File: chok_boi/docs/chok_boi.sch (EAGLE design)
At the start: 13 parts

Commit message: Add gyro and update MOSFETS
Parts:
- removed C_3.3V_IN, C_3.3V_NR, C_BAT: 0.1uF, SparkFun:CAP0603-CAP
- removed C_3.3V_OUT: 10uF, SparkFun:CAP0603-CAP
- removed C_5V: 100uF, SparkFun:CAP0603-CAP
- added B0, B1: (no value), SparkFun-Retired:TAC_SWITCHSMD
- added C_3.3V1: 10uF, SparkFun:CAP0603-CAP
- added C_3.3V2, C_5V1, C_5V11, C_5V4, C_5V5, C_5V6, C_5V7, C_5V8, C_5V9, C_NR, C_NRST, C_VDD1, C_VDD3, C_VDDA1: 0.1uF, SparkFun:CAP0603-CAP
- added C_5V10: 0.01uF, SparkFun:CAP0603-CAP
- added C_5V12: 2.2nF, SparkFun:CAP0603-CAP
- added C_5V2, C_BAT2: 100uF, SparkFun-Passives:CAP1206
- added C_BAT1, C_ELF2, C_ERF2, C_ERF3, C_S2, C_VDD0, C_VDD2: 0.1uF, SparkFun-Capacitors:CAP0603-CAP
- added C_ELF1, C_ERF1, C_ERF4, C_S1: 4.7uF, SparkFun-Capacitors:CAP0603-CAP
- added C_VCAP1, C_VCAP2: 2.2uF, SparkFun:CAP0603-CAP
- added C_VDDA2: 1uF, SparkFun:CAP0603-CAP
- added C_VSS1: 4.7uF, SparkFun:CAP0603-CAP
- added IC1: L293DD, st-microelectronics:L293DD
- added LED1, LED2, LED3: (no value), SparkFun:LED0603
- added LED_PWR: green, SparkFun:LED1206
- added R_B0, R_BOOT1, R_ELF_PD, R_ERF_PD, R_ERF_PD1, R_ES_PD: 47k, SparkFun-Passives:RESISTOR0603-RES
- added R_ELF, R_ERF: 10, SparkFun-Passives:RESISTOR0603-RES
- added R_ES1, R_ES2, R_ES3, R_ES4: 5.6, SparkFun-Passives:RESISTOR0603-RES
- added R_LED1, R_LED2, R_LED3, R_PWR: 1k, SparkFun-Passives:RESISTOR0603-RES
- added R_RLF, R_RLS, R_RRF, R_RRF1, R_RRF2, R_RRS: 1.8k, SparkFun-Passives:RESISTOR0603-RES
- added R_VM1: 20k, SparkFun-Passives:RESISTOR0603-RES
- added R_VM2: 10k, SparkFun-Passives:RESISTOR0603-RES
- added SERIAL1, SERIAL2: (no value), pinhead:PINHD-1X4
- added T1, T2, T3, T4: (no value), zetex:NPNSOT323
- added U$10, U$11, U$13, U$17, U$18, U$19: EMITTER, sfh4550 _ teft4300:EMITTER
- added U$12: FUTURA_V1.0_MOTOR_MOUNT, Futura 1.0 motor mount template:FUTURA_V1.0_MOTOR_MOUNT
- added U$15, U$16: SPLITTER, splitter:SPLITTER
- added U$20, U$21, U$7, U$8, U$9: RECEIVER, sfh4550 _ teft4300:RECEIVER
- added U1: MPU-6000, SparkFun-Sensors:MPU-6000
- L1: device SparkFun:INDUCTOR1007 -> SparkFun-Passives:INDUCTOR1007
- S1: device SparkFun-Switches:SWITCH-SPDT-PTH-11.6X4.0MM -> SparkFun:SWITCH-SPSTPTH
- U$1: value TPS76850(SOIC-8) -> JST_CONNECTOR_FEMALE; device TPS76850(SOIC-8):TPS76850(SOIC-8) -> JST_CONNECTOR_FEMALE. through hole:JST_CONNECTOR_FEMALE
- U$2: value TPS73633(SOT-23) -> JST_CONNECTOR_FEMALE; device TPS73633(SOT-23):TPS73633(SOT-23) -> JST_CONNECTOR_FEMALE. through hole:JST_CONNECTOR_FEMALE
- U$3: value JST_CONNECTOR_FEMALE -> TPS73633(SOT-23); device JST_CONNECTOR_FEMALE. through hole:JST_CONNECTOR_FEMALE -> TPS73633(SOT-23):TPS73633(SOT-23)
- U$4: value JST_CONNECTOR_FEMALE -> TPS76850(SOIC-8); device JST_CONNECTOR_FEMALE. through hole:JST_CONNECTOR_FEMALE -> TPS76850(SOIC-8):TPS76850(SOIC-8)
- U$5: value SPLITTER -> STM32F405/415_LQFP64; device splitter:SPLITTER -> STM32F10x F4xx:STM32F405/415_LQFP64
- U$6: value SPLITTER -> RECEIVER; device splitter:SPLITTER -> sfh4550 _ teft4300:RECEIVER
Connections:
- removed net BAT: C_BAT.1, S1.S, U$1.IN1, U$1.IN2
- new net BATTERY: C_BAT1.1, C_BAT2.1, IC1.VS, R_VM1.2, S1.P, U$4.IN1, U$4.IN2
- new net BOOT0: B0.4, R_B0.1, U$5.BOOT0, U$5.PB5
- new net EM_D: R_ES_PD.2, T2.B, U$5.PA5
- new net EM_LF: R_ELF_PD.2, T1.B, U$5.PC6
- new net EM_RF: R_ERF_PD.2, T3.B, U$5.PA2
- new net EM_S: R_ERF_PD1.2, T4.B
- new net ENC_LA: U$12.L_CHA, U$5.PA15
- new net ENC_LB: U$12.L_CHB, U$5.PB3
- new net ENC_RA: U$12.R_CHA, U$5.PA0_AKUP
- new net ENC_RB: U$12.R_CHB, U$5.PA1
- new net INT: U1.INT
- new net LED1: LED1.A, U$5.PA11
- new net LED2: LED2.A, U$5.PC10
- new net LED3: LED3.A, U$5.PC0
- new net MISO: U1.AD0/SDO
- new net MLB: IC1.OUT1, U$12.L_MOTOR_B
- new net MLF: IC1.OUT2, U$12.L_MOTOR_A
- new net MOSI: U1.SDA/SDI
- new net MRB: IC1.OUT3, U$12.R_MOTOR_B
- new net MRF: IC1.OUT4, U$12.R_MOTOR_A
- new net N$10: R_BOOT1.1, U$5.PB2
- new net N$12: LED1.C, R_LED1.2
- new net N$14: U$18.-, U$19.+
- new net N$15: R_ES3.2, R_ES4.2, U$19.-
- new net N$16: LED2.C, R_LED2.2
- new net N$17: R_ES1.2, R_ES2.2, U$17.-
- new net N$18: R_ES1.1, R_ES2.1, T2.C
- new net N$19: R_ES3.1, R_ES4.1, T4.C
- new net N$20: C_5V11.1, U1.REGOUT
- new net N$21: LED3.C, R_LED3.2
- new net N$22: C_5V12.1, U1.CPOUT
- new net N$23: R_ERF.1, T3.C
- new net N$27: R_ERF.2, U$13.-
- new net N$4: C_VCAP1.2, U$5.VCAP_1
- new net N$5: R_ELF.2, U$10.-
- new net N$6: C_VCAP2.2, U$5.VCAP_2
- new net N$7: R_ELF.1, T1.C
- new net N$8: LED_PWR.A, R_PWR.1
- new net N$9: U$11.-, U$17.+
- new net OUTZ: U$5.PA7
- new net PWMLB: IC1.IN1, U$5.PB7
- new net PWMLF: IC1.IN2, U$5.PB6
- new net PWMRB: IC1.IN3, U$5.PB8
- new net PWMRF: IC1.IN4, U$5.PB9
- new net REC_LD: R_RLS.2, U$5.PC4, U$7.E
- new net REC_LF: R_RLF.2, U$5.PC5, U$6.E
- new net REC_LH: R_RRF2.2, U$21.E
- new net REC_RD: R_RRS.2, U$5.PA6, U$8.E
- new net REC_RF: R_RRF.2, U$5.PA4, U$9.E
- new net REC_RH: R_RRF1.2, U$20.E
- new net RESET: B1.3, C_NRST.1, SERIAL2.4, U$5.NRST
- new net RX: SERIAL1.2, U$5.PA10
- new net SCK: U1.SCL/SCLK
- new net SS1: U1.CS
- new net SWCLK: SERIAL2.1, U$5.PA14
- new net SWDIO: SERIAL2.3, U$5.PA13
- new net TX: SERIAL1.1, U$5.PA9
- new net VOLTMETER: R_VM1.1, R_VM2.2, U$5.PA3
- net 3.3V: now also B0.1, C_3.3V1.1, C_3.3V2.1, C_VDD0.2, C_VDD1.2, C_VDD2.1, C_VDD3.1, C_VSS1.1, L1.1, SERIAL1.4, U$3.OUT, U$5.VBAT, U$5.VDD_0, U$5.VDD_1, U$5.VDD_2, U$5.VDD_3; no longer C_3.3V_OUT.1, L1.2, U$2.OUT
- net 5V: now also C_5V1.1, C_5V2.1, C_ELF1.1, C_ELF2.1, C_ERF1.1, C_ERF2.1, C_ERF3.1, C_ERF4.1, C_S1.1, C_S2.1, IC1.EN1, IC1.EN2, IC1.VSS, R_PWR.2, U$10.+, U$11.+, U$12.L_VCC, U$12.R_VCC, U$13.+, U$18.+, U$3.EN, U$3.IN, U$4.OUT1, U$4.OUT2; no longer C_3.3V_IN.1, C_5V.1, U$1.OUT1, U$1.OUT2, U$2.EN, U$2.IN
- net A3.3V: now also C_5V10.1, C_5V4.1, C_5V5.1, C_5V6.1, C_5V7.1, C_5V8.1, C_5V9.1, C_VDDA1.1, C_VDDA2.1, L1.2, U$20.C, U$21.C, U$5.VDDA, U$6.C, U$7.C, U$8.C, U$9.C, U1.VDD; no longer L1.1
- net AGND: now also C_5V10.2, C_5V11.2, C_5V12.2, C_5V4.2, C_5V5.2, C_5V6.2, C_5V7.2, C_5V8.2, C_5V9.2, C_VDDA1.2, C_VDDA2.2, R_RLF.1, R_RLS.1, R_RRF.1, R_RRF1.1, R_RRF2.1, R_RRS.1, U$15.2, U$5.VSSA, U1.GND; no longer U$6.2
- net GND: now also B1.2, C_3.3V1.2, C_3.3V2.2, C_5V1.2, C_5V2.2, C_BAT1.2, C_BAT2.2, C_ELF1.2, C_ELF2.2, C_ERF1.2, C_ERF2.2, C_ERF3.2, C_ERF4.2, C_NR.2, C_NRST.2, C_S1.2, C_S2.2, C_VCAP1.1, C_VCAP2.1, C_VDD0.1, C_VDD1.1, C_VDD2.2, C_VDD3.2, C_VSS1.2, LED_PWR.C, R_B0.2, R_BOOT1.2, R_ELF_PD.1, R_ERF_PD.1, R_ERF_PD1.1, R_ES_PD.1, R_LED1.1, R_LED2.1, R_LED3.1, R_VM2.1, SERIAL1.3, SERIAL2.2, T1.E, T2.E, T3.E, T4.E, U$1.-, U$12.L_GND, U$12.R_GND, U$15.1, U$16.2, U$3.GND, U$4.EN(BAR), U$4.GND, U$5.VSS_0, U$5.VSS_1; no longer C_3.3V_IN.2, C_3.3V_NR.2, C_3.3V_OUT.2, C_5V.2, C_BAT.2, U$1.EN(BAR), U$1.GND, U$2.GND, U$3.-, U$5.2, U$6.1
- net MGND: now also IC1.GND@1, IC1.GND@2, IC1.GND@3, IC1.GND@4, IC1.GND@5, IC1.GND@6, IC1.GND@7, IC1.GND@8, U$16.1; no longer U$5.1
- net N$1: now also U$1.+, U$2.-; no longer U$3.+, U$4.-
- net N$2: now also S1.S, U$2.+; no longer C_3.3V_NR.1, U$2.NR/FB
- net N$3: now also C_NR.1, U$3.NR/FB; no longer S1.P, U$4.+
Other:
- note added: "Batteries"
- moved on the sheet: L1, S1

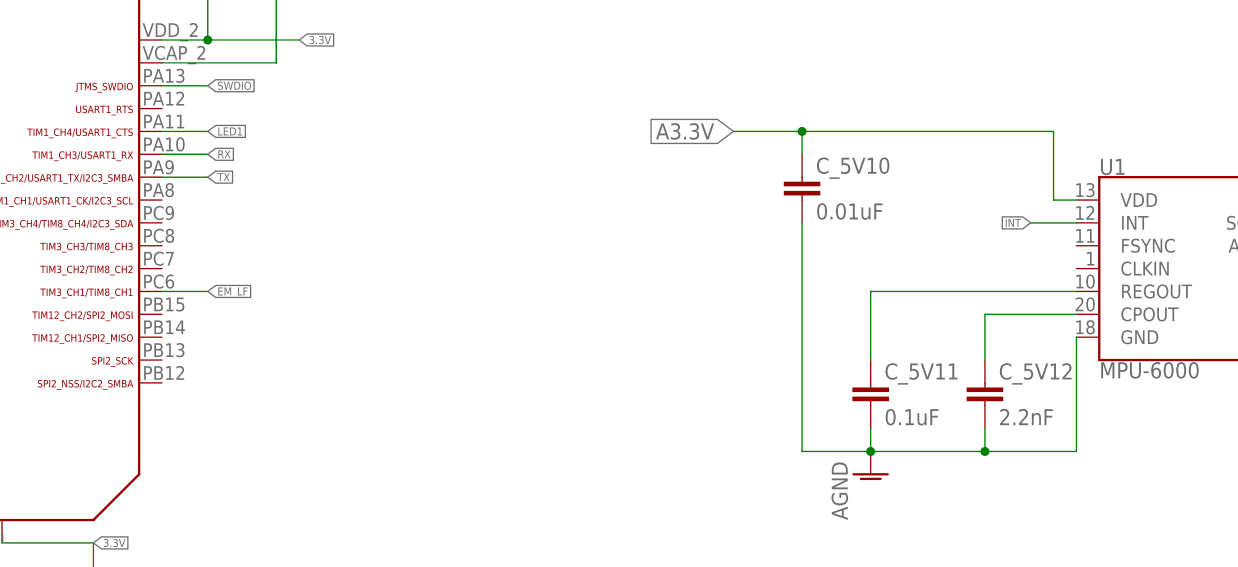
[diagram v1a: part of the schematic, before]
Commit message: Add gitignore and finish gyro connections
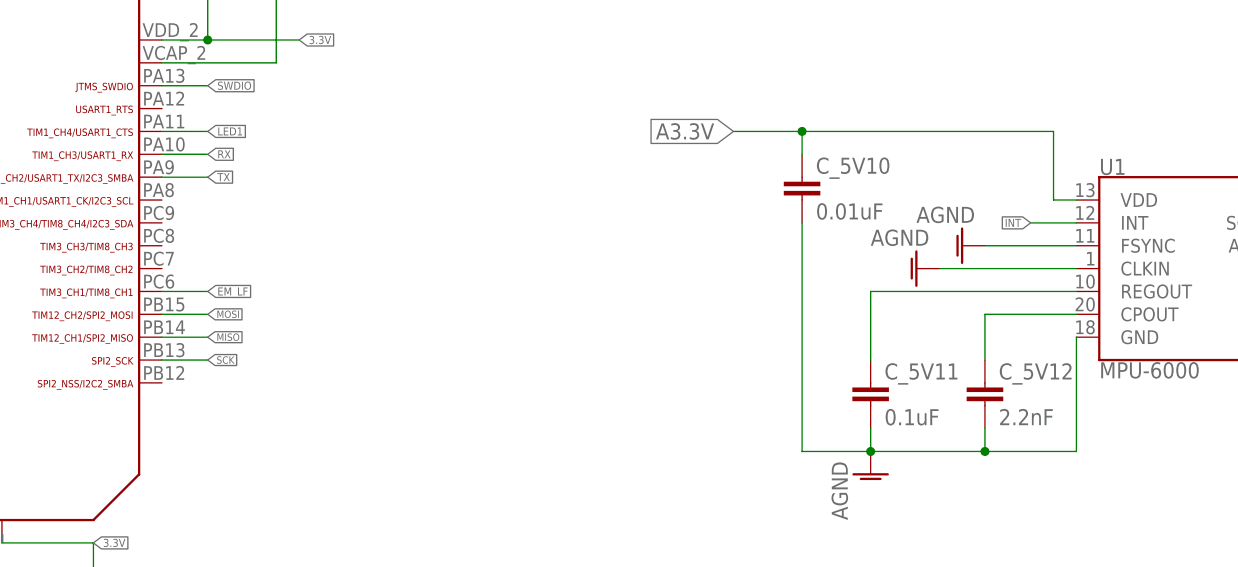
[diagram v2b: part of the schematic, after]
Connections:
- net AGND: now also U1.CLKIN, U1.FSYNC
- net MISO: now also U$5.PB14
- net MOSI: now also U$5.PB15
- net SCK: now also U$5.PB13
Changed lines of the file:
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@@
 <?xml version="1.0" encoding="utf-8"?>
 <!DOCTYPE eagle SYSTEM "eagle.dtd">
-<eagle version="8.3.2">
+<eagle version="8.4.1">
 <drawing>
 <settings>
@@
 <part name="T3" library="zetex" library_urn="urn:adsk.eagle:library:418" deviceset="NPNSOT323" device="" package3d_urn="urn:adsk.eagle:package:30986/1"/>
 <part name="T4" library="zetex" library_urn="urn:adsk.eagle:library:418" deviceset="NPNSOT323" device="" package3d_urn="urn:adsk.eagle:package:30986/1"/>
+<part name="AGND2" library="supply1" library_urn="urn:adsk.eagle:library:371" deviceset="AGND" device=""/>
+<part name="AGND6" library="supply1" library_urn="urn:adsk.eagle:library:371" deviceset="AGND" device=""/>
 </parts>
 <sheets>
@@
 <instance part="T3" gate="A" x="281.94" y="-63.5"/>
 <instance part="T4" gate="A" x="332.74" y="-63.5"/>
+<instance part="AGND2" gate="VR1" x="33.02" y="-76.2" rot="R270"/>
+<instance part="AGND6" gate="VR1" x="27.94" y="-78.74" rot="R270"/>
 </instances>
 <busses>
@@
 <pinref part="AGND5" gate="VR1" pin="AGND"/>
 </segment>
+<segment>
+<pinref part="U1" gate="G$1" pin="FSYNC"/>
+<wire x1="45.72" y1="-76.2" x2="35.56" y2="-76.2" width="0.1524" layer="91"/>
+<pinref part="AGND2" gate="VR1" pin="AGND"/>
+</segment>
+<segment>
+<pinref part="U1" gate="G$1" pin="CLKIN"/>
+<wire x1="45.72" y1="-78.74" x2="30.48" y2="-78.74" width="0.1524" layer="91"/>
+<pinref part="AGND6" gate="VR1" pin="AGND"/>
+</segment>
 </net>
 <net name="REC_RD" class="0">
@@
 <label x="83.82" y="-73.66" size="0.889" layer="95" xref="yes"/>
 </segment>
+<segment>
+<pinref part="U$5" gate="G$1" pin="PB13"/>
+<wire x1="-55.88" y1="-88.9" x2="-50.8" y2="-88.9" width="0.1524" layer="91"/>
+<label x="-50.8" y="-88.9" size="0.8128" layer="95" xref="yes"/>
+</segment>
 </net>
 <net name="MISO" class="0">
@@
 <label x="83.82" y="-76.2" size="0.889" layer="95" xref="yes"/>
 </segment>
+<segment>
+<pinref part="U$5" gate="G$1" pin="PB14"/>
+<wire x1="-55.88" y1="-86.36" x2="-50.8" y2="-86.36" width="0.1524" layer="91"/>
+<label x="-50.8" y="-86.36" size="0.8128" layer="95" xref="yes"/>
+</segment>
 </net>
 <net name="MOSI" class="0">
@@
 <label x="83.82" y="-78.74" size="0.889" layer="95" xref="yes"/>
 </segment>
-</net>
+<segment>
+<pinref part="U$5" gate="G$1" pin="PB15"/>
+<wire x1="-55.88" y1="-83.82" x2="-50.8" y2="-83.82" width="0.1524" layer="91"/>
+<label x="-50.8" y="-83.82" size="0.8128" layer="95" xref="yes"/>
+</segment>
+</net>

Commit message: Finish rec/led pair schematic
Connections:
- removed net EM_S: R_ERF_PD1.2, T4.B
- removed net OUTZ: U$5.PA7
- new net EM_H: R_ERF_PD1.2, T4.B, U$5.PA7
- net REC_LH: now also U$5.PB1
- net REC_RH: now also U$5.PB0
- net SS1: now also U$5.PC8
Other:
- moved on the sheet: C_VCAP1, R_BOOT1
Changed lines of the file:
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@@
 <instance part="C_VDD2" gate="G$1" x="-50.8" y="-43.18" rot="R180"/>
 <instance part="GND8" gate="1" x="-50.8" y="-33.02" rot="R180"/>
-<instance part="C_VCAP1" gate="G$1" x="-76.2" y="-116.84" rot="R180"/>
+<instance part="C_VCAP1" gate="G$1" x="-76.2" y="-121.92" rot="R180"/>
 <instance part="C_VDD1" gate="G$1" x="-63.5" y="-116.84" rot="R180"/>
-<instance part="GND9" gate="1" x="-63.5" y="-129.54"/>
+<instance part="GND9" gate="1" x="-63.5" y="-142.24"/>
 <instance part="C_VDDA2" gate="G$1" x="-165.1" y="-78.74" rot="R180"/>
 <instance part="C_VDDA1" gate="G$1" x="-149.86" y="-78.74" rot="R180"/>
@@
 <instance part="SERIAL1" gate="A" x="-203.2" y="-40.64"/>
 <instance part="SERIAL2" gate="A" x="-223.52" y="-40.64"/>
-<instance part="R_BOOT1" gate="G$1" x="-83.82" y="-119.38" rot="R270"/>
+<instance part="R_BOOT1" gate="G$1" x="-83.82" y="-132.08" rot="R270"/>
 <instance part="U$18" gate="G$1" x="335.28" y="-20.32"/>
 <instance part="U$19" gate="G$1" x="335.28" y="-35.56"/>
@@
 <segment>
 <pinref part="C_VCAP1" gate="G$1" pin="1"/>
-<wire x1="-76.2" y1="-121.92" x2="-76.2" y2="-127" width="0.1524" layer="91"/>
+<wire x1="-76.2" y1="-127" x2="-76.2" y2="-139.7" width="0.1524" layer="91"/>
 <pinref part="C_VDD1" gate="G$1" pin="1"/>
-<wire x1="-63.5" y1="-121.92" x2="-63.5" y2="-127" width="0.1524" layer="91"/>
-<wire x1="-63.5" y1="-127" x2="-76.2" y2="-127" width="0.1524" layer="91"/>
+<wire x1="-63.5" y1="-121.92" x2="-63.5" y2="-139.7" width="0.1524" layer="91"/>
+<wire x1="-63.5" y1="-139.7" x2="-76.2" y2="-139.7" width="0.1524" layer="91"/>
 <pinref part="GND9" gate="1" pin="GND"/>
-<junction x="-63.5" y="-127"/>
-<wire x1="-83.82" y1="-127" x2="-76.2" y2="-127" width="0.1524" layer="91"/>
-<junction x="-76.2" y="-127"/>
+<junction x="-63.5" y="-139.7"/>
+<wire x1="-83.82" y1="-139.7" x2="-76.2" y2="-139.7" width="0.1524" layer="91"/>
+<junction x="-76.2" y="-139.7"/>
 <pinref part="R_BOOT1" gate="G$1" pin="2"/>
-<wire x1="-83.82" y1="-124.46" x2="-83.82" y2="-127" width="0.1524" layer="91"/>
+<wire x1="-83.82" y1="-137.16" x2="-83.82" y2="-139.7" width="0.1524" layer="91"/>
 </segment>
 <segment>
@@
 <pinref part="U$5" gate="G$1" pin="VCAP_1"/>
 <pinref part="C_VCAP1" gate="G$1" pin="2"/>
-<wire x1="-76.2" y1="-109.22" x2="-76.2" y2="-114.3" width="0.1524" layer="91"/>
-</segment>
-</net>
-<net name="OUTZ" class="0">
-<segment>
-<pinref part="U$5" gate="G$1" pin="PA7"/>
-<wire x1="-96.52" y1="-109.22" x2="-96.52" y2="-114.3" width="0.1524" layer="91"/>
-<label x="-96.52" y="-114.3" size="0.889" layer="95" rot="R270" xref="yes"/>
+<wire x1="-76.2" y1="-109.22" x2="-76.2" y2="-119.38" width="0.1524" layer="91"/>
 </segment>
 </net>
@@
 <pinref part="U$5" gate="G$1" pin="PB2"/>
 <pinref part="R_BOOT1" gate="G$1" pin="1"/>
-<wire x1="-83.82" y1="-109.22" x2="-83.82" y2="-114.3" width="0.1524" layer="91"/>
+<wire x1="-83.82" y1="-109.22" x2="-83.82" y2="-127" width="0.1524" layer="91"/>
 </segment>
 </net>
@@
 <label x="309.88" y="48.26" size="1.778" layer="95" rot="R180" xref="yes"/>
 </segment>
+<segment>
+<pinref part="U$5" gate="G$1" pin="PB0"/>
+<wire x1="-88.9" y1="-109.22" x2="-88.9" y2="-114.3" width="0.1524" layer="91"/>
+<label x="-88.9" y="-114.3" size="0.8128" layer="95" rot="R270" xref="yes"/>
+</segment>
 </net>
 <net name="REC_LH" class="0">
@@
 <label x="350.52" y="48.26" size="1.778" layer="95" rot="R180" xref="yes"/>
 </segment>
-</net>
-<net name="EM_S" class="0">
+<segment>
+<pinref part="U$5" gate="G$1" pin="PB1"/>
+<wire x1="-86.36" y1="-109.22" x2="-86.36" y2="-114.3" width="0.1524" layer="91"/>
+<label x="-86.36" y="-114.3" size="0.8128" layer="95" rot="R270" xref="yes"/>
+</segment>
+</net>
+<net name="EM_H" class="0">
 <segment>
 <pinref part="R_ERF_PD1" gate="G$1" pin="2"/>
@@
 <junction x="322.58" y="-63.5"/>
 </segment>
+<segment>
+<pinref part="U$5" gate="G$1" pin="PA7"/>
+<wire x1="-96.52" y1="-109.22" x2="-96.52" y2="-114.3" width="0.1524" layer="91"/>
+<label x="-96.52" y="-114.3" size="0.8128" layer="95" rot="R270" xref="yes"/>
+</segment>
 </net>
 <net name="N$20" class="0">
@@
 <label x="83.82" y="-71.12" size="0.889" layer="95" xref="yes"/>
 </segment>
-</net>
+<segment>
+<pinref part="U$5" gate="G$1" pin="PC8"/>
+<wire x1="-55.88" y1="-76.2" x2="-50.8" y2="-76.2" width="0.1524" layer="91"/>
+<label x="-50.8" y="-76.2" size="0.8128" layer="95" xref="yes"/>
+</segment>
+</net>

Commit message: Place all big components on board
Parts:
- renumbered U$10 to LEFT_FRONT_EMITTER, U$6 to REC_LF
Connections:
- net N$14 renamed H_EM
- net N$15 renamed H2_EM
- net N$17 renamed D2_EM
- net N$27 renamed RF_EM
- net N$5 renamed LF_EM
- net N$9 renamed D_EM
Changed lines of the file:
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@@
 <part name="C_NR" library="SparkFun" deviceset="CAP" device="0603-CAP" value="0.1uF"/>
 <part name="U$5" library="STM32F10x F4xx" deviceset="STM32F405/415_LQFP64" device=""/>
-<part name="U$6" library="sfh4550 _ teft4300" deviceset="RECEIVER" device=""/>
+<part name="REC_LF" library="sfh4550 _ teft4300" deviceset="RECEIVER" device=""/>
 <part name="C_BAT2" library="SparkFun-Passives" deviceset="CAP" device="1206" value="100uF"/>
 <part name="R_RLF" library="SparkFun-Passives" deviceset="RESISTOR" device="0603-RES" value="1.8k"/>
@@
 <part name="U$9" library="sfh4550 _ teft4300" deviceset="RECEIVER" device=""/>
 <part name="R_RRF" library="SparkFun-Passives" deviceset="RESISTOR" device="0603-RES" value="1.8k"/>
-<part name="U$10" library="sfh4550 _ teft4300" deviceset="EMITTER" device=""/>
+<part name="LEFT_FRONT_EMITTER" library="sfh4550 _ teft4300" deviceset="EMITTER" device=""/>
 <part name="R_ELF" library="SparkFun-Passives" deviceset="RESISTOR" device="0603-RES" value="10"/>
 <part name="R_ELF_PD" library="SparkFun-Passives" deviceset="RESISTOR" device="0603-RES" value="47k"/>
@@
 <instance part="C_NR" gate="G$1" x="68.58" y="-5.08"/>
 <instance part="U$5" gate="G$1" x="-93.98" y="-73.66" rot="R270"/>
-<instance part="U$6" gate="G$1" x="160.02" y="58.42"/>
+<instance part="REC_LF" gate="G$1" x="160.02" y="58.42"/>
 <instance part="C_BAT2" gate="G$1" x="35.56" y="33.02"/>
 <instance part="R_RLF" gate="G$1" x="162.56" y="40.64" rot="R90"/>
@@
 <instance part="U$9" gate="G$1" x="266.7" y="58.42"/>
 <instance part="R_RRF" gate="G$1" x="269.24" y="40.64" rot="R90"/>
-<instance part="U$10" gate="G$1" x="162.56" y="-27.94"/>
+<instance part="LEFT_FRONT_EMITTER" gate="G$1" x="162.56" y="-27.94"/>
 <instance part="R_ELF" gate="G$1" x="162.56" y="-45.72" rot="R90"/>
 <instance part="R_ELF_PD" gate="G$1" x="144.78" y="-73.66" rot="R90"/>
@@
 <wire x1="218.44" y1="-15.24" x2="218.44" y2="-10.16" width="0.1524" layer="91"/>
 <wire x1="284.48" y1="-10.16" x2="233.68" y2="-10.16" width="0.1524" layer="91"/>
-<pinref part="U$10" gate="G$1" pin="+"/>
+<pinref part="LEFT_FRONT_EMITTER" gate="G$1" pin="+"/>
 <wire x1="233.68" y1="-10.16" x2="218.44" y2="-10.16" width="0.1524" layer="91"/>
 <wire x1="162.56" y1="-22.86" x2="162.56" y2="-10.16" width="0.1524" layer="91"/>
@@
 <net name="REC_LF" class="0">
 <segment>
-<pinref part="U$6" gate="G$1" pin="E"/>
+<pinref part="REC_LF" gate="G$1" pin="E"/>
 <pinref part="R_RLF" gate="G$1" pin="2"/>
 <wire x1="162.56" y1="53.34" x2="162.56" y2="48.26" width="0.1524" layer="91"/>
@@
 </segment>
 </net>
-<net name="N$5" class="0">
-<segment>
-<pinref part="U$10" gate="G$1" pin="-"/>
+<net name="LF_EM" class="0">
+<segment>
+<pinref part="LEFT_FRONT_EMITTER" gate="G$1" pin="-"/>
 <pinref part="R_ELF" gate="G$1" pin="2"/>
 <wire x1="162.56" y1="-33.02" x2="162.56" y2="-40.64" width="0.1524" layer="91"/>
-</segment>
-</net>
-<net name="N$17" class="0">
-<segment>
-<pinref part="R_ES1" gate="G$1" pin="2"/>
-<pinref part="R_ES2" gate="G$1" pin="2"/>
-<wire x1="218.44" y1="-45.72" x2="228.6" y2="-45.72" width="0.1524" layer="91"/>
-<pinref part="U$17" gate="G$1" pin="-"/>
-<wire x1="218.44" y1="-40.64" x2="218.44" y2="-45.72" width="0.1524" layer="91"/>
-<junction x="218.44" y="-45.72"/>
 </segment>
 </net>
@@
 </segment>
 </net>
-<net name="N$27" class="0">
+<net name="RF_EM" class="0">
 <segment>
 <pinref part="U$13" gate="G$1" pin="-"/>
@@
 <wire x1="195.58" y1="71.12" x2="195.58" y2="63.5" width="0.1524" layer="91"/>
 <junction x="195.58" y="71.12"/>
-<pinref part="U$6" gate="G$1" pin="C"/>
+<pinref part="REC_LF" gate="G$1" pin="C"/>
 <wire x1="162.56" y1="71.12" x2="162.56" y2="63.5" width="0.1524" layer="91"/>
 <junction x="162.56" y="71.12"/>
@@
 </segment>
 </net>
-<net name="N$9" class="0">
+<net name="D_EM" class="0">
 <segment>
 <pinref part="U$11" gate="G$1" pin="-"/>
@@
 </segment>
 </net>
-<net name="N$14" class="0">
+<net name="H_EM" class="0">
 <segment>
 <pinref part="U$18" gate="G$1" pin="-"/>
 <pinref part="U$19" gate="G$1" pin="+"/>
 <wire x1="335.28" y1="-25.4" x2="335.28" y2="-30.48" width="0.1524" layer="91"/>
-</segment>
-</net>
-<net name="N$15" class="0">
-<segment>
-<pinref part="U$19" gate="G$1" pin="-"/>
-<pinref part="R_ES3" gate="G$1" pin="2"/>
-<wire x1="335.28" y1="-40.64" x2="335.28" y2="-45.72" width="0.1524" layer="91"/>
-<pinref part="R_ES4" gate="G$1" pin="2"/>
-<wire x1="335.28" y1="-45.72" x2="345.44" y2="-45.72" width="0.1524" layer="91"/>
-<junction x="335.28" y="-45.72"/>
 </segment>
 </net>
@@
 </segment>
 </net>
+<net name="D2_EM" class="0">
+<segment>
+<pinref part="R_ES1" gate="G$1" pin="2"/>
+<pinref part="R_ES2" gate="G$1" pin="2"/>
+<wire x1="218.44" y1="-45.72" x2="228.6" y2="-45.72" width="0.1524" layer="91"/>
+<pinref part="U$17" gate="G$1" pin="-"/>
+<wire x1="218.44" y1="-40.64" x2="218.44" y2="-45.72" width="0.1524" layer="91"/>
+<junction x="218.44" y="-45.72"/>
+</segment>
+</net>
+<net name="H2_EM" class="0">
+<segment>
+<pinref part="U$19" gate="G$1" pin="-"/>
+<pinref part="R_ES3" gate="G$1" pin="2"/>
+<wire x1="335.28" y1="-40.64" x2="335.28" y2="-45.72" width="0.1524" layer="91"/>
+<pinref part="R_ES4" gate="G$1" pin="2"/>
+<wire x1="335.28" y1="-45.72" x2="345.44" y2="-45.72" width="0.1524" layer="91"/>
+<junction x="335.28" y="-45.72"/>
+</segment>
+</net>

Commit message: Change part names for easier routing
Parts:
- renumbered C_5V4 to C_REC_LD, C_5V5 to C_REC_RD, C_5V6 to C_REC_RF, C_5V7 to C_REC_RH, C_5V8 to C_REC_LH, C_5V9 to C_REC_LF, C_ERF3 to C_E_H2, C_ERF4 to C_E_H1, C_S1 to C_EM_D1, C_S2 to C_EM_D2, R_ES1 to R_ED1, R_ES2 to R_ED2, R_ES3 to R_EH1, R_ES4 to R_EH2, R_RLS to R_RLD, R_RRF1 to R_RRH, R_RRF2 to R_RLH, R_RRS to R_RRD
